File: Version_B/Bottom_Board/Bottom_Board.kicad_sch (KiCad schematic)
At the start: 13 parts, among them J1 Conn_02x03_Top_Bottom, J2 Conn_02x03_Top_Bottom, J3 Conn_01x02_Pin, J4 Screw_Terminal_01x05, J5 DIN-5, J6 Conn_01x02_Pin, J7 Conn_01x02_Pin, J8 Screw_Terminal_01x04, SW2 SW_DIP_x04

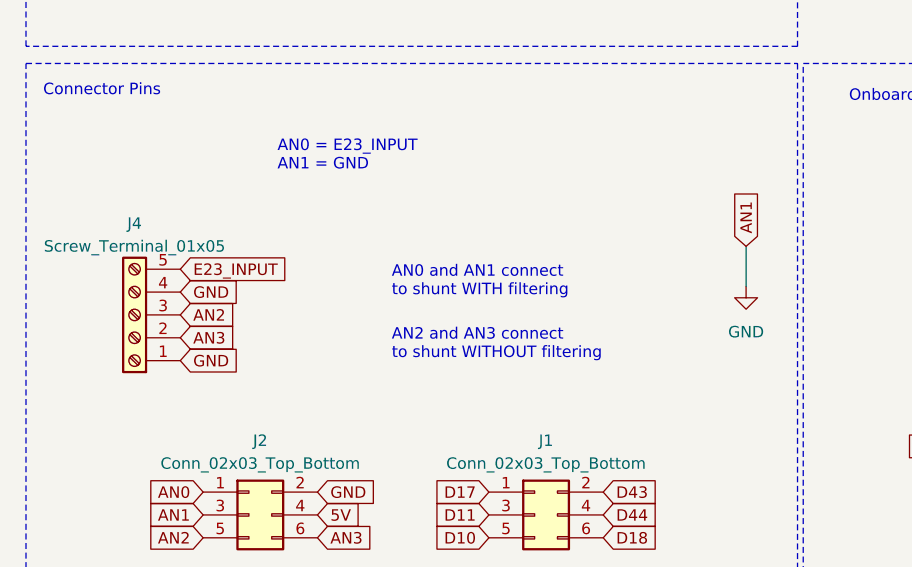
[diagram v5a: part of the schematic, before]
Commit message: changed 5 pin to 4 pin term block
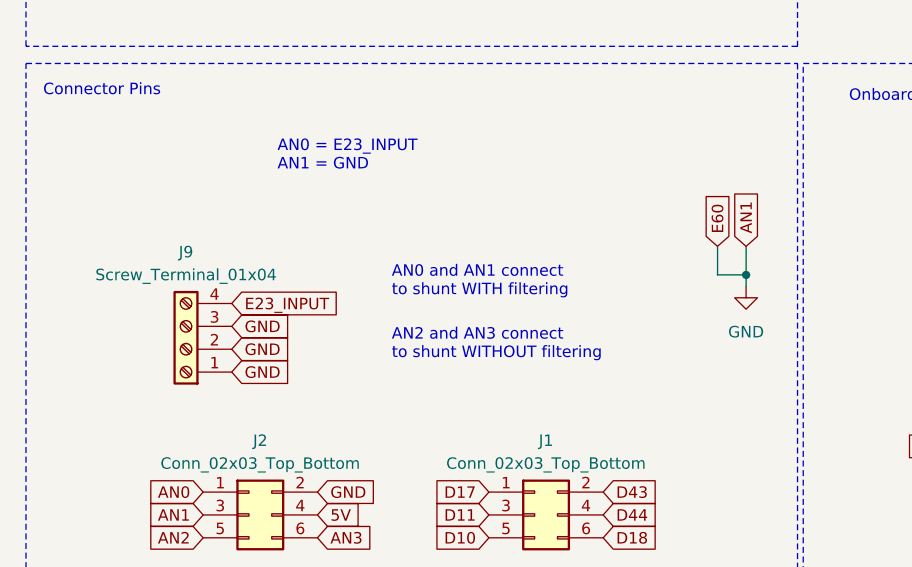
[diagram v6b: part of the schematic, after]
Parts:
- removed J4: Screw_Terminal_01x05, bot_lib:BarrierStrip_1x05_P8.26mm_3.25in_Vertical, symbol Connector:Screw_Terminal_01x05
- added J9: Screw_Terminal_01x04, bot_lib:Terminal_Strip_4_Pin, symbol Connector:Screw_Terminal_01x04
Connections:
- net E23_INPUT: now also J9.4 (Pin_4)
- net GND: now also J9.1 (Pin_1), J9.2 (Pin_2), J9.3 (Pin_3)
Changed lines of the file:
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@@
   (junction (at 81.915 120.65) (diameter 0) (color 0 0 0 0)
   )
+  (junction (at 97.79 160.02) (diameter 0) (color 0 0 0 0)
+  )
   (junction (at 81.915 110.49) (diameter 0) (color 0 0 0 0)
   )
+  (wire (pts (xy 97.79 160.02) (xy 97.79 161.29))
+    (stroke (width 0) (type default))
+  )
   (wire (pts (xy 25.4 45.72) (xy 29.845 45.72))
     (stroke (width 0) (type default))
   )
-  (wire (pts (xy 97.79 156.845) (xy 97.79 161.29))
+  (wire (pts (xy 97.79 156.845) (xy 97.79 160.02))
     (stroke (width 0) (type default))
   )
@@
     (stroke (width 0) (type default))
   )
+  (wire (pts (xy 94.615 156.845) (xy 94.615 160.02))
+    (stroke (width 0) (type default))
+  )
   (wire (pts (xy 81.915 123.19) (xy 81.915 120.65))
     (stroke (width 0) (type default))
@@
   )
   (wire (pts (xy 29.845 48.26) (xy 29.845 51.435))
+    (stroke (width 0) (type default))
+  )
+  (wire (pts (xy 94.615 160.02) (xy 97.79 160.02))
     (stroke (width 0) (type default))
   )
@@
     )
   )
-  (global_label "GND" (shape input) (at 34.925 169.545 0) (fields_autoplaced)
-    (effects (font (size 1.27 1.27)) (justify left))
-    (property "Intersheetrefs" "${INTERSHEET_REFS}" (at 41.7013 169.545 0)
-      (effects (font (size 1.27 1.27)) (justify left) hide)
-    )
-  )
   (global_label "D10" (shape input) (at 127.635 161.29 180) (fields_autoplaced)
     (effects (font (size 1.27 1.27)) (justify right))
@@
     )
   )
+  (global_label "E23_INPUT" (shape input) (at 40.64 163.195 0) (fields_autoplaced)
+    (effects (font (size 1.27 1.27)) (justify left))
+    (property "Intersheetrefs" "${INTERSHEET_REFS}" (at 53.5848 163.195 0)
+      (effects (font (size 1.27 1.27)) (justify left) hide)
+    )
+  )
   (global_label "COM" (shape input) (at 41.91 109.22 270) (fields_autoplaced)
     (effects (font (size 1.27 1.27)) (justify right))
@@
     )
   )
-  (global_label "GND" (shape input) (at 34.925 161.925 0) (fields_autoplaced)
-    (effects (font (size 1.27 1.27)) (justify left))
-    (property "Intersheetrefs" "${INTERSHEET_REFS}" (at 41.7013 161.925 0)
-      (effects (font (size 1.27 1.27)) (justify left) hide)
-    )
-  )
-  (global_label "AN3" (shape input) (at 34.925 167.005 0) (fields_autoplaced)
-    (effects (font (size 1.27 1.27)) (justify left))
-    (property "Intersheetrefs" "${INTERSHEET_REFS}" (at 41.4594 167.005 0)
-      (effects (font (size 1.27 1.27)) (justify left) hide)
-    )
-  )
   (global_label "5V" (shape input) (at 34.29 99.06 180) (fields_autoplaced)
     (effects (font (size 1.27 1.27)) (justify right))
@@
     )
   )
-  (global_label "E23_INPUT" (shape input) (at 34.925 159.385 0) (fields_autoplaced)
-    (effects (font (size 1.27 1.27)) (justify left))
-    (property "Intersheetrefs" "${INTERSHEET_REFS}" (at 47.8698 159.385 0)
+  (global_label "GND" (shape input) (at 40.64 165.735 0) (fields_autoplaced)
+    (effects (font (size 1.27 1.27)) (justify left))
+    (property "Intersheetrefs" "${INTERSHEET_REFS}" (at 47.4163 165.735 0)
+      (effects (font (size 1.27 1.27)) (justify left) hide)
+    )
+  )
+  (global_label "E60" (shape input) (at 94.615 156.845 90) (fields_autoplaced)
+    (effects (font (size 1.27 1.27)) (justify left))
+    (property "Intersheetrefs" "${INTERSHEET_REFS}" (at 94.615 150.3712 90)
       (effects (font (size 1.27 1.27)) (justify left) hide)
     )
@@
     )
   )
-  (global_label "AN2" (shape input) (at 34.925 164.465 0) (fields_autoplaced)
-    (effects (font (size 1.27 1.27)) (justify left))
-    (property "Intersheetrefs" "${INTERSHEET_REFS}" (at 41.4594 164.465 0)
+  (global_label "GND" (shape input) (at 40.64 170.815 0) (fields_autoplaced)
+    (effects (font (size 1.27 1.27)) (justify left))
+    (property "Intersheetrefs" "${INTERSHEET_REFS}" (at 47.4163 170.815 0)
+      (effects (font (size 1.27 1.27)) (justify left) hide)
+    )
+  )
+  (global_label "GND" (shape input) (at 40.64 168.275 0) (fields_autoplaced)
+    (effects (font (size 1.27 1.27)) (justify left))
+    (property "Intersheetrefs" "${INTERSHEET_REFS}" (at 47.4163 168.275 0)
       (effects (font (size 1.27 1.27)) (justify left) hide)
     )
@@
     (property "Intersheetrefs" "${INTERSHEET_REFS}" (at 56.4877 99.06 0)
       (effects (font (size 1.27 1.27)) (justify left) hide)
+    )
+  )
+  (symbol (lib_id "Connector:Screw_Terminal_01x04") (at 35.56 168.275 180) (unit 1)
+    (in_bom yes) (on_board yes) (dnp no) (fields_autoplaced)
+    (property "Reference" "J9" (at 35.56 157.48 0)
+      (effects (font (size 1.27 1.27)))
+    )
+    (property "Value" "Screw_Terminal_01x04" (at 35.56 160.02 0)
+      (effects (font (size 1.27 1.27)))
+    )
+    (property "Footprint" "bot_lib:Terminal_Strip_4_Pin" (at 35.56 168.275 0)
+      (effects (font (size 1.27 1.27)) hide)
+    )
+    (property "Datasheet" "~" (at 35.56 168.275 0)
+      (effects (font (size 1.27 1.27)) hide)
+    )
+    (pin "1")
+    (pin "2")
+    (pin "3")
+    (pin "4")
+    (instances
+      (project "Bottom_Board"
+        (path "/5ce934df-ced0-4773-94af-75275ecebb9b"
+          (reference "J9") (unit 1)
+        )
+      )
     )
   )
@@
         )
       )
-    )
-  )
-  (symbol (lib_id "Connector:Screw_Terminal_01x05") (at 29.845 164.465 180) (unit 1)
-    (in_bom yes) (on_board yes) (dnp no) (fields_autoplaced)
-    (property "Reference" "J4" (at 29.845 154.305 0)
-      (effects (font (size 1.27 1.27)))
-    )
-    (property "Value" "Screw_Terminal_01x05" (at 29.845 156.845 0)
-      (effects (font (size 1.27 1.27)))
-    )
-    (property "Footprint" "bot_lib:BarrierStrip_1x05_P8.26mm_3.25in_Vertical" (at 29.845 164.465 0)
-      (effects (font (size 1.27 1.27)) hide)
-    )
-    (property "Datasheet" "~" (at 29.845 164.465 0)
-      (effects (font (size 1.27 1.27)) hide)
-    )
-    (pin "1")
-    (pin "2")
-    (pin "3")
-    (pin "4")
-    (pin "5")
-    (instances
-      (project "Bottom_Board"
-        (path "/5ce934df-ced0-4773-94af-75275ecebb9b"
-          (reference "J4") (unit 1)
-        )
-      )

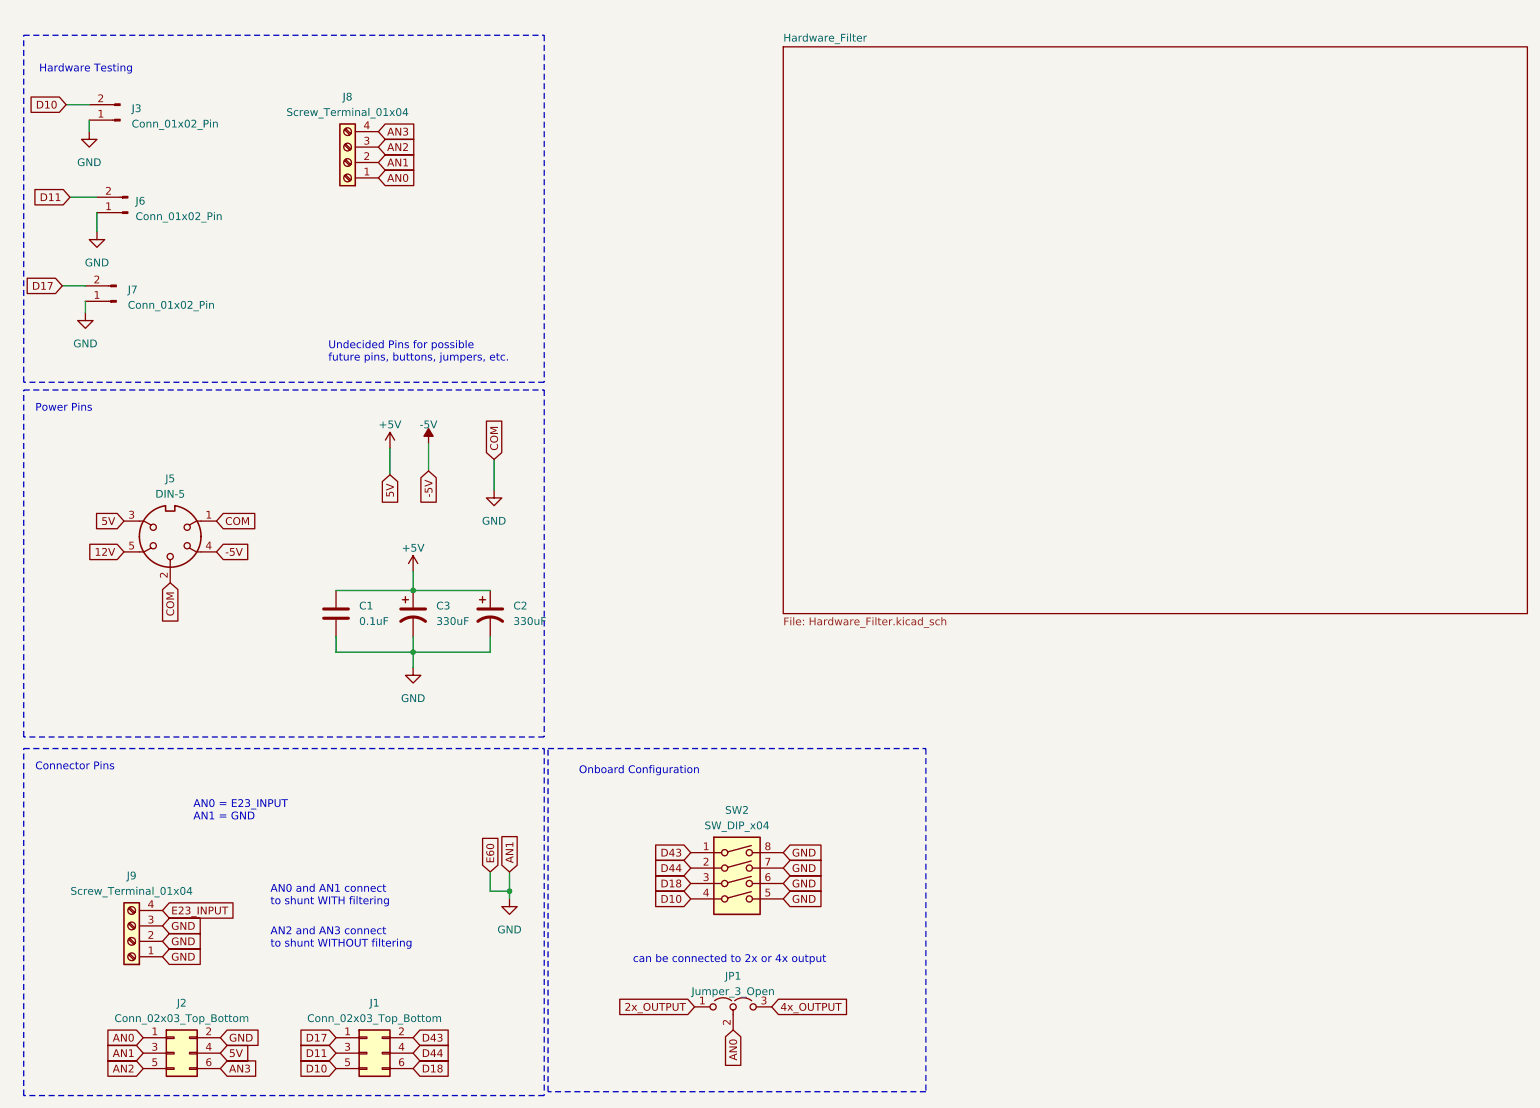
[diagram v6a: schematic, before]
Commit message: ads1015 on bottom board and aesthetic changes
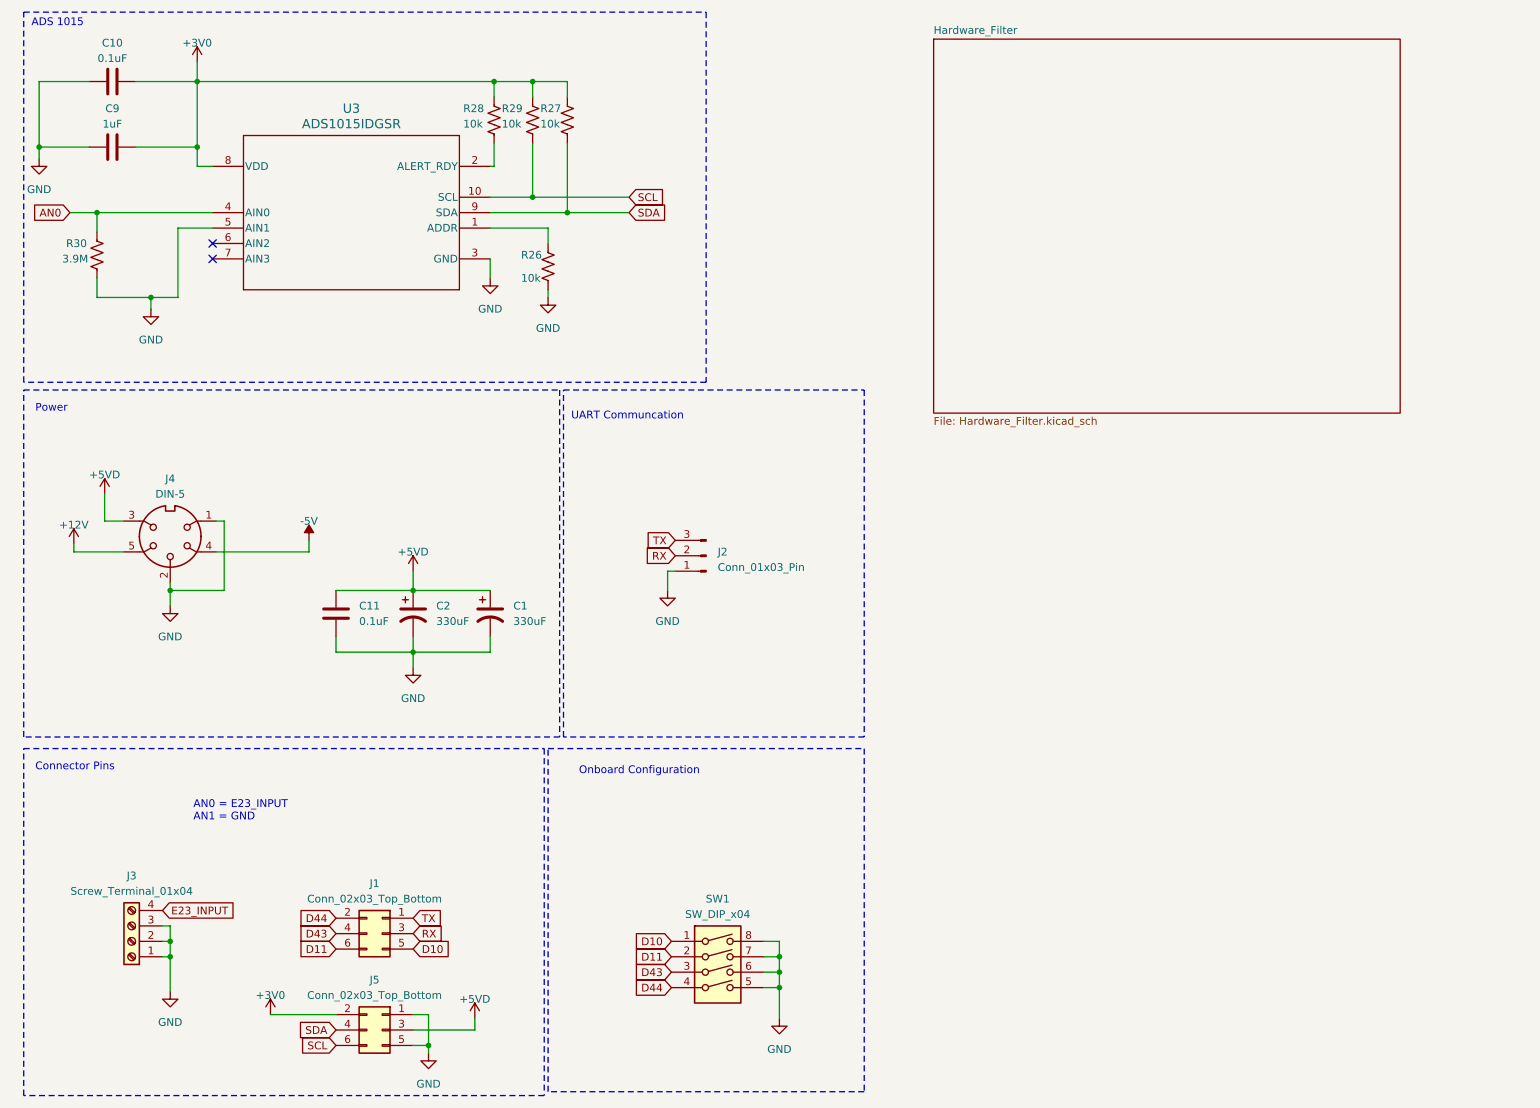
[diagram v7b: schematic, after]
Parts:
- removed J3, J6, J7: Conn_01x02_Pin, Connector_PinSocket_2.54mm:PinSocket_1x02_P2.54mm_Vertical, symbol Connector:Conn_01x02_Pin
- removed J8: Screw_Terminal_01x04, Connector_PinHeader_2.54mm:PinHeader_1x04_P2.54mm_Vertical, symbol Connector:Screw_Terminal_01x04
- removed JP1: Jumper_3_Open, Connector_PinHeader_2.54mm:PinHeader_1x03_P2.54mm_Vertical, symbol Jumper:Jumper_3_Open
- added C10: 0.1uF, Capacitor_SMD:C_0603_1608Metric, symbol Device:C
- added C9: 1uF, Capacitor_SMD:C_0603_1608Metric, symbol Device:C
- added J2: Conn_01x03_Pin, Connector_PinHeader_2.54mm:PinHeader_1x03_P2.54mm_Vertical, symbol Connector:Conn_01x03_Pin
- added R26, R27, R28, R29: 10k, Resistor_SMD:R_0603_1608Metric, symbol Device:R_US
- added R30: 3.9M, Resistor_SMD:R_0603_1608Metric, symbol Device:R_US
- added U3: ADS1015IDGSR, bot_lib:DGS0010A_N, symbol ads1015:ADS1015IDGSR
- J1: renamed from J2; footprint Connector_PinSocket_2.54mm:PinSocket_2x03_P2.54mm_Vertical -> bot_lib:PinSocket_2x03_P2.54mm_Vertical
- J5: renamed from J1; footprint Connector_PinSocket_2.54mm:PinSocket_2x03_P2.54mm_Vertical -> bot_lib:PinSocket_2x03_P2.54mm_Vertical
- renumbered C2 to C1, C1 to C11, C3 to C2, J9 to J3, J5 to J4, SW2 to SW1
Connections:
- net AN2 is gone; now on net D10: J1.5 (Pin_5)
- net AN3 is gone; now on net D11: J1.6 (Pin_6)
- net D17 is gone; now on net GND: J5.1 (Pin_1)
- net AN0: now also R30.1, U3.4 (AIN0); no longer J1.1 (Pin_1)
- net D10: now also SW1.1; no longer J5.5 (Pin_5), SW1.4
- net D11: now also SW1.2; no longer J5.3 (Pin_3)
- net D43: now also J1.4 (Pin_4), SW1.3; no longer J5.2 (Pin_2), SW1.1
- net D44: now also J1.2 (Pin_2), SW1.4; no longer J5.4 (Pin_4), SW1.2
- net GND: now also J5.5 (Pin_5), C10.1, C9.1, J2.1 (Pin_1), R26.2, R30.2, U3.3 (GND), U3.5 (AIN1); no longer J1.2 (Pin_2), J1.3 (Pin_3)
- net +5V renamed +5VD
- net +5VD: now also J5.3 (Pin_3); no longer J1.4 (Pin_4)
- net 12V renamed +12V
- net D18 renamed SCL
- net SCL: now also R29.2, U3.10 (SCL); no longer SW1.3
- new net: R26.1, U3.1 (ADDR)
- new net: R28.2, U3.2 (ALERT_RDY)
- new net +3V0: C10.2, C9.2, J5.2 (Pin_2), R27.1, R28.1, R29.1, U3.8 (VDD)
- new net RX: J1.3 (Pin_3), J2.2 (Pin_2)
- new net SDA: J5.4 (Pin_4), R27.2, U3.9 (SDA)
- new net TX: J1.1 (Pin_1), J2.3 (Pin_3)
- no-connect marks 0 -> 2
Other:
- note added: "ADS 1015"
- note added: "Power"
- note added: "UART Communcation"
- note removed: "AN0 and AN1 connect to shunt WITH filtering"
- note removed: "AN2 and AN3 connect to shunt WITHOUT filtering"
- note removed: "Hardware Testing"
- note removed: "Power Pins"
- note removed: "Undecided Pins for possible future pins, buttons, jumpers, etc."
- note removed: "can be connected to 2x or 4x output"
- company: (none) -> Secured Solutions Group
- title: (none) -> Monitoring System (Bottom Board)
- moved on the sheet: J1, J5, SW1
